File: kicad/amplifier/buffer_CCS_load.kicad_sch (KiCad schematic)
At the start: 3 parts, among them Q9 DN2540

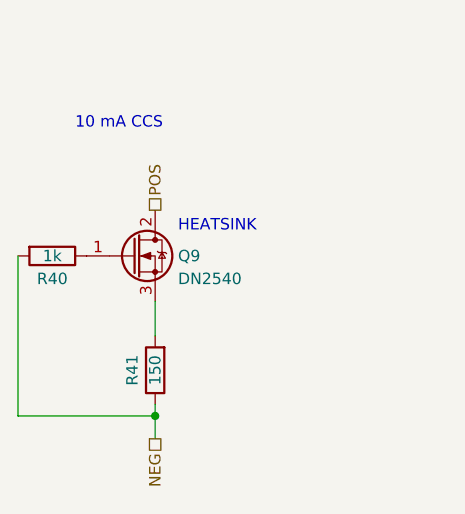
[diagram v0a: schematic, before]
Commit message: Add protection diode to buffer CCS, PCB fixes
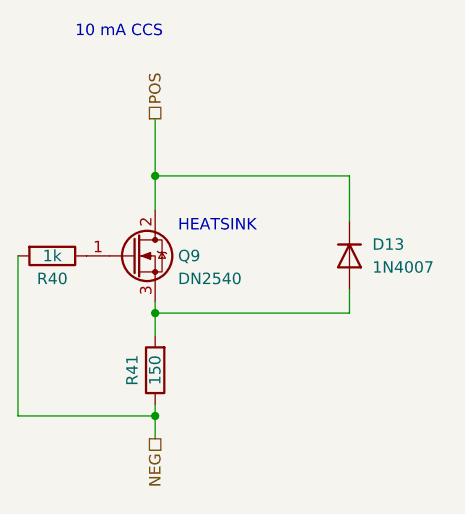
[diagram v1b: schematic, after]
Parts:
- added D13: 1N4007, Diode_THT:D_DO-41_SOD81_P10.16mm_Horizontal, symbol Diode:1N4007
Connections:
- net POS: now also D13.1 (K)
- net at Q9.3 (S), R41.2: now also D13.2 (A)
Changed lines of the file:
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@@
 	(paper "A4")
+	(junction
+		(at 137.16 76.2)
+		(diameter 0)
+		(color 0 0 0 0)
+	)
 	(junction
 		(at 137.16 102.87)
@@
 		(color 0 0 0 0)
 	)
+	(junction
+		(at 137.16 91.44)
+		(diameter 0)
+		(color 0 0 0 0)
+	)
+	(wire
+		(pts
+			(xy 137.16 91.44) (xy 137.16 90.17)
+		)
+		(stroke
+			(width 0)
+			(type default)
+		)
+	)
 	(wire
 		(pts
@@
 	(wire
 		(pts
+			(xy 158.75 88.9) (xy 158.75 91.44)
+		)
+		(stroke
+			(width 0)
+			(type default)
+		)
+	)
+	(wire
+		(pts
+			(xy 158.75 91.44) (xy 137.16 91.44)
+		)
+		(stroke
+			(width 0)
+			(type default)
+		)
+	)
+	(wire
+		(pts
+			(xy 158.75 76.2) (xy 137.16 76.2)
+		)
+		(stroke
+			(width 0)
+			(type default)
+		)
+	)
+	(wire
+		(pts
 			(xy 121.92 85.09) (xy 121.92 102.87)
 		)
@@
 	(wire
 		(pts
+			(xy 137.16 76.2) (xy 137.16 80.01)
+		)
+		(stroke
+			(width 0)
+			(type default)
+		)
+	)
+	(wire
+		(pts
+			(xy 137.16 69.85) (xy 137.16 76.2)
+		)
+		(stroke
+			(width 0)
+			(type default)
+		)
+	)
+	(wire
+		(pts
 			(xy 121.92 102.87) (xy 137.16 102.87)
 		)
@@
 	(wire
 		(pts
-			(xy 137.16 93.98) (xy 137.16 90.17)
+			(xy 158.75 81.28) (xy 158.75 76.2)
+		)
+		(stroke
+			(width 0)
+			(type default)
+		)
+	)
+	(wire
+		(pts
+			(xy 137.16 93.98) (xy 137.16 91.44)
 		)
 		(stroke
@@
 	(text "10 mA CCS"
 		(exclude_from_sim no)
-		(at 128.27 71.12 0)
+		(at 128.27 60.96 0)
 		(effects
 			(font
@@
 	(hierarchical_label "POS"
 		(shape passive)
-		(at 137.16 80.01 90)
+		(at 137.16 69.85 90)
 		(fields_autoplaced yes)
 		(effects
@@
 		(instances
 			(project "OSDEHA_AMP"
+				(path "/59cc4414-299b-49db-9f9a-b06f69a12073/117f0db4-f368-407f-8708-b67954482099"
+					(reference "R43")
+					(unit 1)
+				)
 				(path "/59cc4414-299b-49db-9f9a-b06f69a12073/964c5f27-279d-4094-beed-423757c37563"
 					(reference "R41")
 					(unit 1)
 				)
+			)
+		)
+	)
+	(symbol
+		(lib_id "Diode:1N4007")
+		(at 158.75 85.09 270)
+		(unit 1)
+		(exclude_from_sim no)
+		(in_bom yes)
+		(on_board yes)
+		(dnp no)
+		(fields_autoplaced yes)
+		(property "Reference" "D13"
+			(at 161.29 83.8199 90)
+			(effects
+				(font
+					(size 1.27 1.27)
+				)
+				(justify left)
+			)
+		)
+		(property "Value" "1N4007"
+			(at 161.29 86.3599 90)
+			(effects
+				(font
+					(size 1.27 1.27)
+				)
+				(justify left)
+			)
+		)
+		(property "Footprint" "Diode_THT:D_DO-41_SOD81_P10.16mm_Horizontal"
+			(at 154.305 85.09 0)
+			(effects
+				(font
+					(size 1.27 1.27)
+				)
+				(hide yes)
+			)
+		)
+		(property "Datasheet" "http://www.vishay.com/docs/88503/1n4001.pdf"
+			(at 158.75 85.09 0)
+			(effects
+				(font
+					(size 1.27 1.27)
+				)
+				(hide yes)
+			)
+		)
+		(property "Description" "1000V 1A General Purpose Rectifier Diode, DO-41"
+			(at 158.75 85.09 0)
+			(effects
+				(font
+					(size 1.27 1.27)
+				)
+				(hide yes)
+			)
+		)
+		(property "Sim.Device" "D"
+			(at 158.75 85.09 0)
+			(effects
+				(font
+					(size 1.27 1.27)
+				)
+				(hide yes)
+			)
+		)
+		(property "Sim.Pins" "1=K 2=A"
+			(at 158.75 85.09 0)
+			(effects
+				(font
+					(size 1.27 1.27)
+				)
+				(hide yes)
+			)
+		)
+		(pin "2"
+		)
+		(pin "1"
+		)
+		(instances
+			(project ""
 				(path "/59cc4414-299b-49db-9f9a-b06f69a12073/117f0db4-f368-407f-8708-b67954482099"
-					(reference "R43")
+					(reference "D14")
+					(unit 1)
+				)
+				(path "/59cc4414-299b-49db-9f9a-b06f69a12073/964c5f27-279d-4094-beed-423757c37563"
+					(reference "D13")
 					(unit 1)
 				)
@@
 		(instances
 			(project "OSDEHA_AMP"
+				(path "/59cc4414-299b-49db-9f9a-b06f69a12073/117f0db4-f368-407f-8708-b67954482099"
+					(reference "R42")
+					(unit 1)
+				)
 				(path "/59cc4414-299b-49db-9f9a-b06f69a12073/964c5f27-279d-4094-beed-423757c37563"
 					(reference "R40")
-					(unit 1)
-				)
-				(path "/59cc4414-299b-49db-9f9a-b06f69a12073/117f0db4-f368-407f-8708-b67954482099"
-					(reference "R42")
 					(unit 1)
 				)
@@
 		(instances
 			(project "OSDEHA_AMP"
+				(path "/59cc4414-299b-49db-9f9a-b06f69a12073/117f0db4-f368-407f-8708-b67954482099"
+					(reference "Q10")
+					(unit 1)
+				)
 				(path "/59cc4414-299b-49db-9f9a-b06f69a12073/964c5f27-279d-4094-beed-423757c37563"
 					(reference "Q9")
 					(unit 1)
 				)
-				(path "/59cc4414-299b-49db-9f9a-b06f69a12073/117f0db4-f368-407f-8708-b67954482099"
-					(reference "Q10")
-					(unit 1)
-				)

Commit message: up
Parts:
- removed D13: 1N4007, Diode_THT:D_DO-41_SOD81_P10.16mm_Horizontal, symbol Diode:1N4007
- R43: renamed from R41; value 150 -> 536
- renumbered Q9 to Q10, R40 to R42
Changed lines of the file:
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@@
 	(paper "A4")
-	(junction
-		(at 137.16 76.2)
-		(diameter 0)
-		(color 0 0 0 0)
-	)
 	(junction
 		(at 137.16 102.87)
@@
 		(color 0 0 0 0)
 	)
-	(junction
-		(at 137.16 91.44)
-		(diameter 0)
-		(color 0 0 0 0)
-	)
-	(wire
-		(pts
-			(xy 137.16 91.44) (xy 137.16 90.17)
+	(wire
+		(pts
+			(xy 137.16 90.17) (xy 137.16 93.98)
 		)
 		(stroke
@@
 	(wire
 		(pts
-			(xy 158.75 88.9) (xy 158.75 91.44)
-		)
-		(stroke
-			(width 0)
-			(type default)
-		)
-	)
-	(wire
-		(pts
-			(xy 158.75 91.44) (xy 137.16 91.44)
-		)
-		(stroke
-			(width 0)
-			(type default)
-		)
-	)
-	(wire
-		(pts
-			(xy 158.75 76.2) (xy 137.16 76.2)
-		)
-		(stroke
-			(width 0)
-			(type default)
-		)
-	)
-	(wire
-		(pts
 			(xy 121.92 85.09) (xy 121.92 102.87)
 		)
@@
 	(wire
 		(pts
-			(xy 137.16 76.2) (xy 137.16 80.01)
-		)
-		(stroke
-			(width 0)
-			(type default)
-		)
-	)
-	(wire
-		(pts
-			(xy 137.16 69.85) (xy 137.16 76.2)
+			(xy 137.16 69.85) (xy 137.16 80.01)
 		)
 		(stroke
@@
 		(pts
 			(xy 137.16 102.87) (xy 137.16 105.41)
-		)
-		(stroke
-			(width 0)
-			(type default)
-		)
-	)
-	(wire
-		(pts
-			(xy 158.75 81.28) (xy 158.75 76.2)
-		)
-		(stroke
-			(width 0)
-			(type default)
-		)
-	)
-	(wire
-		(pts
-			(xy 137.16 93.98) (xy 137.16 91.44)
 		)
 		(stroke
@@
 		(on_board yes)
 		(dnp no)
-		(property "Reference" "R41"
+		(property "Reference" "R43"
 			(at 134.62 97.79 90)
 			(effects
@@
 			)
 		)
-		(property "Value" "150"
+		(property "Value" "536"
 			(at 137.16 97.79 90)
 			(effects
@@
 	)
 	(symbol
-		(lib_id "Diode:1N4007")
-		(at 158.75 85.09 270)
+		(lib_id "Device:R")
+		(at 125.73 85.09 270)
 		(unit 1)
 		(exclude_from_sim no)
@@
 		(on_board yes)
 		(dnp no)
-		(fields_autoplaced yes)
-		(property "Reference" "D13"
-			(at 161.29 83.8199 90)
-			(effects
-				(font
-					(size 1.27 1.27)
-				)
-				(justify left)
-			)
-		)
-		(property "Value" "1N4007"
-			(at 161.29 86.3599 90)
-			(effects
-				(font
-					(size 1.27 1.27)
-				)
-				(justify left)
-			)
-		)
-		(property "Footprint" "Diode_THT:D_DO-41_SOD81_P10.16mm_Horizontal"
-			(at 154.305 85.09 0)
-			(effects
-				(font
-					(size 1.27 1.27)
-				)
-				(hide yes)
-			)
-		)
-		(property "Datasheet" "http://www.vishay.com/docs/88503/1n4001.pdf"
-			(at 158.75 85.09 0)
-			(effects
-				(font
-					(size 1.27 1.27)
-				)
-				(hide yes)
-			)
-		)
-		(property "Description" "1000V 1A General Purpose Rectifier Diode, DO-41"
-			(at 158.75 85.09 0)
-			(effects
-				(font
-					(size 1.27 1.27)
-				)
-				(hide yes)
-			)
-		)
-		(property "Sim.Device" "D"
-			(at 158.75 85.09 0)
-			(effects
-				(font
-					(size 1.27 1.27)
-				)
-				(hide yes)
-			)
-		)
-		(property "Sim.Pins" "1=K 2=A"
-			(at 158.75 85.09 0)
-			(effects
-				(font
-					(size 1.27 1.27)
-				)
-				(hide yes)
-			)
-		)
-		(pin "2"
-		)
-		(pin "1"
-		)
-		(instances
-			(project ""
-				(path "/59cc4414-299b-49db-9f9a-b06f69a12073/117f0db4-f368-407f-8708-b67954482099"
-					(reference "D14")
-					(unit 1)
-				)
-				(path "/59cc4414-299b-49db-9f9a-b06f69a12073/964c5f27-279d-4094-beed-423757c37563"
-					(reference "D13")
-					(unit 1)
-				)
-			)
-		)
-	)
-	(symbol
-		(lib_id "Device:R")
-		(at 125.73 85.09 270)
-		(unit 1)
-		(exclude_from_sim no)
-		(in_bom yes)
-		(on_board yes)
-		(dnp no)
-		(property "Reference" "R40"
+		(property "Reference" "R42"
 			(at 125.73 87.63 90)
 			(effects
@@
 		(on_board yes)
 		(dnp no)
-		(property "Reference" "Q9"
+		(property "Reference" "Q10"
 			(at 139.7 85.09 0)
 			(effects

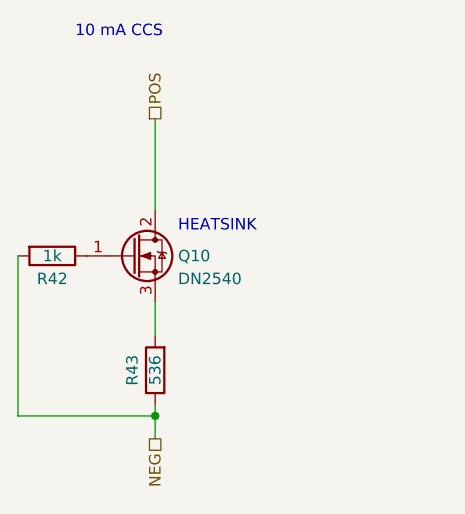
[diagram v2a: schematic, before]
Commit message: safety resistors / fusibles
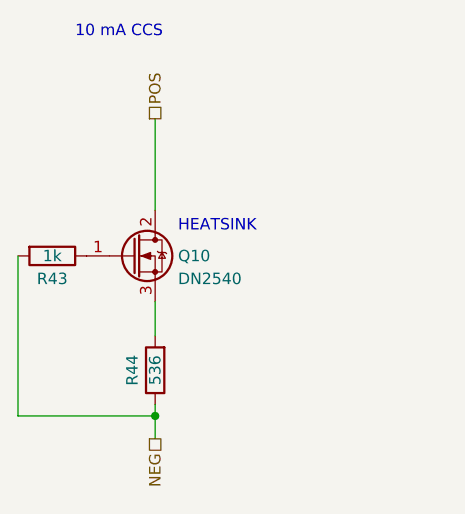
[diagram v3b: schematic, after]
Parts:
- renumbered R42 to R43, R43 to R44
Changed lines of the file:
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@@
 		(on_board yes)
 		(dnp no)
-		(property "Reference" "R43"
+		(property "Reference" "R44"
 			(at 134.62 97.79 90)
 			(effects
@@
 			(project "OSDEHA_AMP"
 				(path "/59cc4414-299b-49db-9f9a-b06f69a12073/117f0db4-f368-407f-8708-b67954482099"
-					(reference "R43")
+					(reference "R44")
 					(unit 1)
 				)
 				(path "/59cc4414-299b-49db-9f9a-b06f69a12073/964c5f27-279d-4094-beed-423757c37563"
-					(reference "R41")
+					(reference "R42")
 					(unit 1)
 				)
@@
 		(on_board yes)
 		(dnp no)
-		(property "Reference" "R42"
+		(property "Reference" "R43"
 			(at 125.73 87.63 90)
 			(effects
@@
 			(project "OSDEHA_AMP"
 				(path "/59cc4414-299b-49db-9f9a-b06f69a12073/117f0db4-f368-407f-8708-b67954482099"
-					(reference "R42")
+					(reference "R43")
 					(unit 1)
 				)
 				(path "/59cc4414-299b-49db-9f9a-b06f69a12073/964c5f27-279d-4094-beed-423757c37563"
-					(reference "R40")
+					(reference "R41")
 					(unit 1)
 				)

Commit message: update CCS sense resistors (LTP, buffers)
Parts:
- R44: MPN CMF55150R00 -> CMF55536R00
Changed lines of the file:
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@@
 			)
 		)
-		(property "MPN" "CMF55150R00"
+		(property "MPN" "CMF55536R00"
 			(at 137.16 97.79 90)
 			(effects

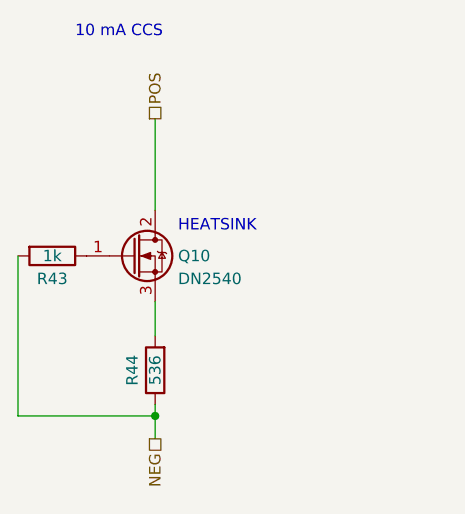
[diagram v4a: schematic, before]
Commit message: doc: CCS sense resistor values, issue #13
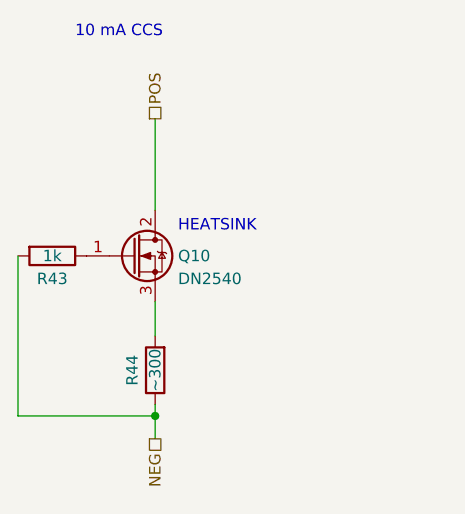
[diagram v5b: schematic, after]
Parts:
- R44: value 536 -> ~300; MPN CMF55536R00 -> CMF55
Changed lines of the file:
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@@
 		(shape passive)
 		(at 137.16 105.41 270)
-		(fields_autoplaced yes)
 		(effects
 			(font
@@
 		(shape passive)
 		(at 137.16 69.85 90)
-		(fields_autoplaced yes)
 		(effects
 			(font
@@
 			)
 		)
-		(property "Value" "536"
+		(property "Value" "~300"
 			(at 137.16 97.79 90)
 			(effects
@@
 			)
 		)
-		(property "Description" ""
+		(property "Description" "Adjust value for CCS current"
 			(at 137.16 97.79 0)
 			(effects
@@
 			)
 		)
-		(property "MPN" "CMF55536R00"
+		(property "MPN" "CMF55"
 			(at 137.16 97.79 90)
 			(effects

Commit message: CCS resistors default values
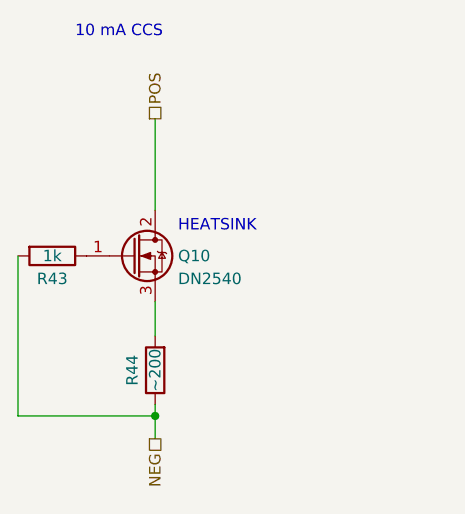
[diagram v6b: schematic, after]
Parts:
- R44: value ~300 -> ~200
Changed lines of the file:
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@@
 			)
 		)
-		(property "Value" "~300"
+		(property "Value" "~200"
 			(at 137.16 97.79 90)
 			(effects

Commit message: CCS resistor value ranges / #13 #14
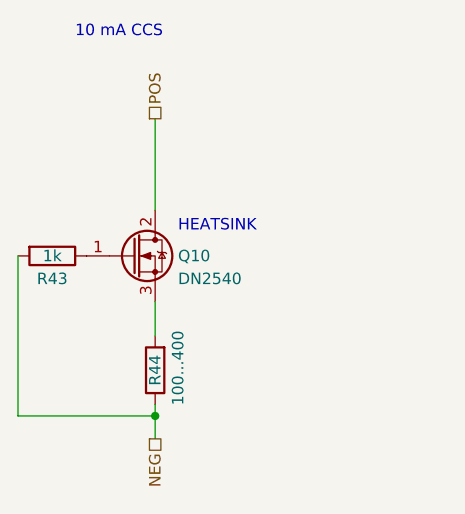
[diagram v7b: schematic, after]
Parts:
- R44: value ~200 -> 100...400
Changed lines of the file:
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@@
 		(dnp no)
 		(property "Reference" "R44"
-			(at 134.62 97.79 90)
+			(at 137.16 97.79 90)
 			(effects
 				(font
@@
 			)
 		)
-		(property "Value" "~200"
-			(at 137.16 97.79 90)
+		(property "Value" "100...400"
+			(at 139.7 97.536 90)
 			(effects
 				(font

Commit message: fix errors in BIAS HV supply
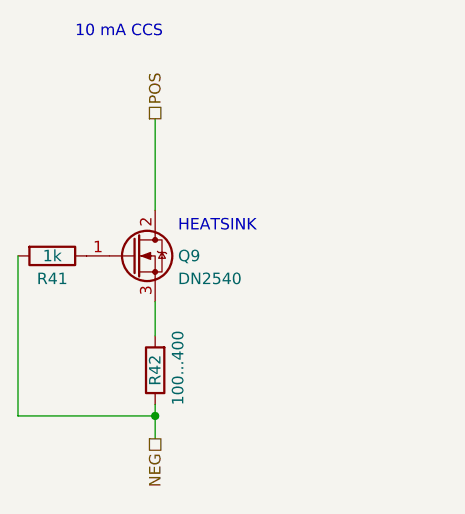
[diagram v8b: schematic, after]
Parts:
- renumbered Q10 to Q9, R43 to R41, R44 to R42
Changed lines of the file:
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@@
 (kicad_sch
-	(version 20231120)
+	(version 20250114)
 	(generator "eeschema")
-	(generator_version "8.0")
+	(generator_version "9.0")
 	(paper "A4")
+	(text "10 mA CCS"
+		(exclude_from_sim no)
+		(at 128.27 60.96 0)
+		(effects
+			(font
+				(size 1.27 1.27)
+			)
+			(justify left bottom)
+		)
+	)
+	(text "HEATSINK"
+		(exclude_from_sim no)
+		(at 139.7 82.55 0)
+		(effects
+			(font
+				(size 1.27 1.27)
+			)
+			(justify left bottom)
+		)
+	)
 	(junction
 		(at 137.16 102.87)
@@
 		)
 	)
-	(text "10 mA CCS"
-		(exclude_from_sim no)
-		(at 128.27 60.96 0)
-		(effects
-			(font
-				(size 1.27 1.27)
-			)
-			(justify left bottom)
-		)
-	)
-	(text "HEATSINK"
-		(exclude_from_sim no)
-		(at 139.7 82.55 0)
-		(effects
-			(font
-				(size 1.27 1.27)
-			)
-			(justify left bottom)
-		)
-	)
 	(hierarchical_label "NEG"
 		(shape passive)
@@
 		(on_board yes)
 		(dnp no)
-		(property "Reference" "R44"
+		(property "Reference" "R42"
 			(at 137.16 97.79 90)
 			(effects
@@
 		(on_board yes)
 		(dnp no)
-		(property "Reference" "R43"
+		(property "Reference" "R41"
 			(at 125.73 87.63 90)
 			(effects
@@
 		(on_board yes)
 		(dnp no)
-		(property "Reference" "Q10"
+		(property "Reference" "Q9"
 			(at 139.7 85.09 0)
 			(effects
